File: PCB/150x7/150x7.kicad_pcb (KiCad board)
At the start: 2 copper layers, 14.5 x 14.5 mm, 51 parts, among them J1 Conn_01x03, J2 Conn_01x03

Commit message: Some tracks
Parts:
- moved C1 18.8 mm to (102.6, 85.3)
- moved C10 18.8 mm to (110.6, 99.7)
- moved C11 18.8 mm to (112.6, 85.3)
- moved C12 18.8 mm to (112.6, 99.7)
- moved C13 18.8 mm to (114.6, 85.3)
- moved C14 18.8 mm to (114.6, 99.7)
- moved C2 18.8 mm to (102.6, 99.7)
- moved C3 18.8 mm to (104.6, 85.3)
- moved C4 18.8 mm to (104.6, 99.7)
- moved C5 18.8 mm to (106.6, 85.3)
- moved C6 18.8 mm to (106.6, 99.7)
- moved C7 18.8 mm to (108.6, 85.3)
- moved C8 18.8 mm to (108.6, 99.7)
- moved C9 18.8 mm to (110.6, 85.3)
- moved D1 18.8 mm to (102.6, 86.5)
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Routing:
- net (no net): track 0.00 -> 23.9 mm

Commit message: power
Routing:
- net (no net): track 23.9 -> 772.4 mm

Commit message: Tracking
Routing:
- net (no net): track 772.4 -> 539.8 mm, vias 0 -> 46

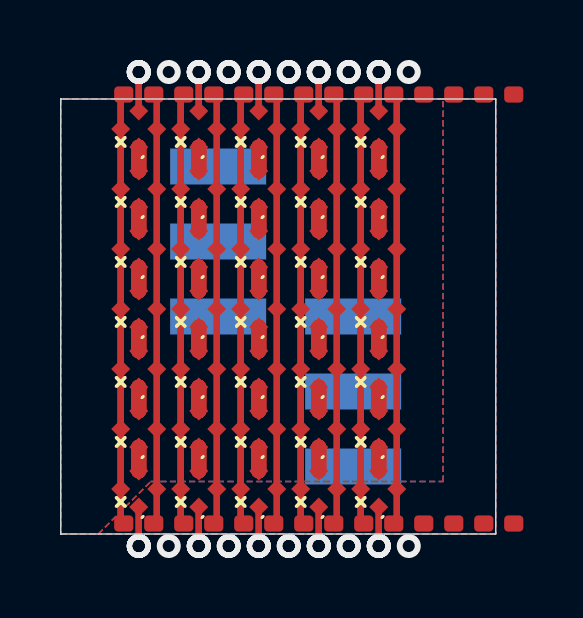
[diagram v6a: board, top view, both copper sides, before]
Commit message: Works - would be nice to have a way to delete the created old entries...
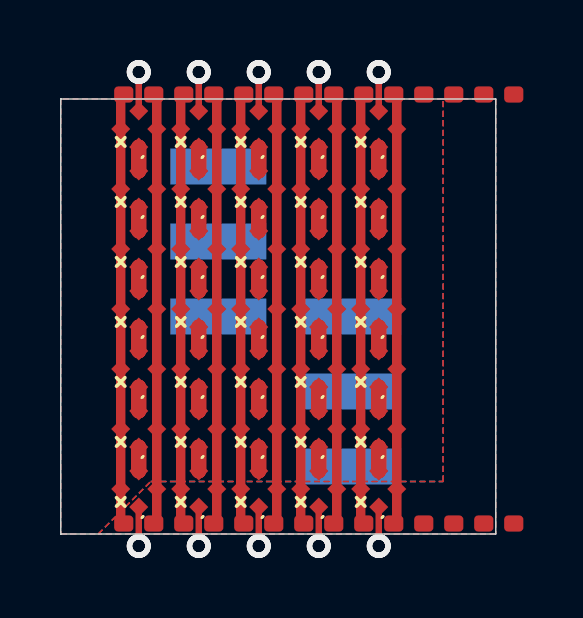
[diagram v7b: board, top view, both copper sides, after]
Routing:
- net (no net): track 539.8 -> 359.9 mm, vias 46 -> 20

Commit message: New layout
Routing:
- net (no net): track 359.9 -> 539.8 mm, vias 20 -> 30
